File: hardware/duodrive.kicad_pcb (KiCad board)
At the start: 2 copper layers, 49 x 75 mm, 92 parts, among them J1 Power, J2 Conn_01x04, J3 Conn_01x03, J4 MP2359, J6 Conn_01x04, J7 Conn_01x04, J8 Conn_01x04, Q1 AOD4184, Q2 AOD4184, Q3 AOD4184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

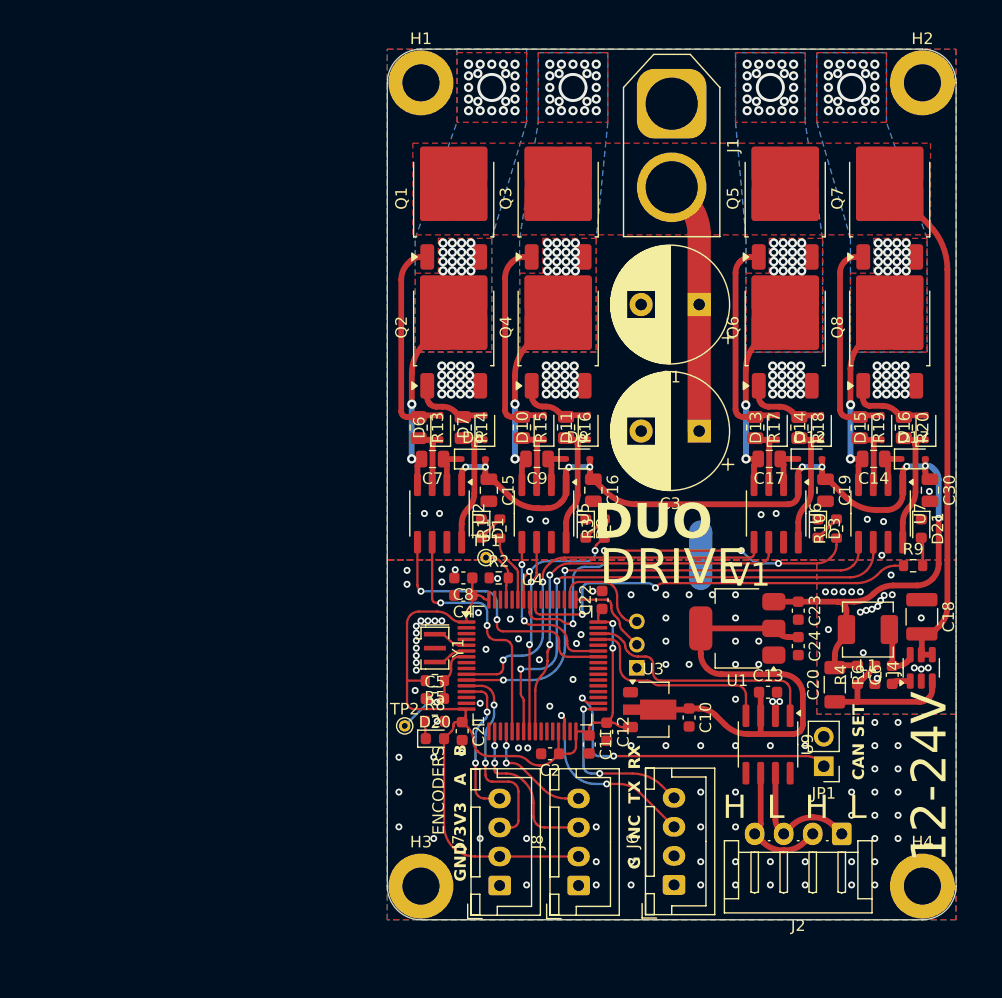
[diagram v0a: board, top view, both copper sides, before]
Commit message: Hardware bug fix
Fixed buck converter output bulk capacitor not connected to ground
Added pull up resistor at buck EN pin instead of connect it to VCC
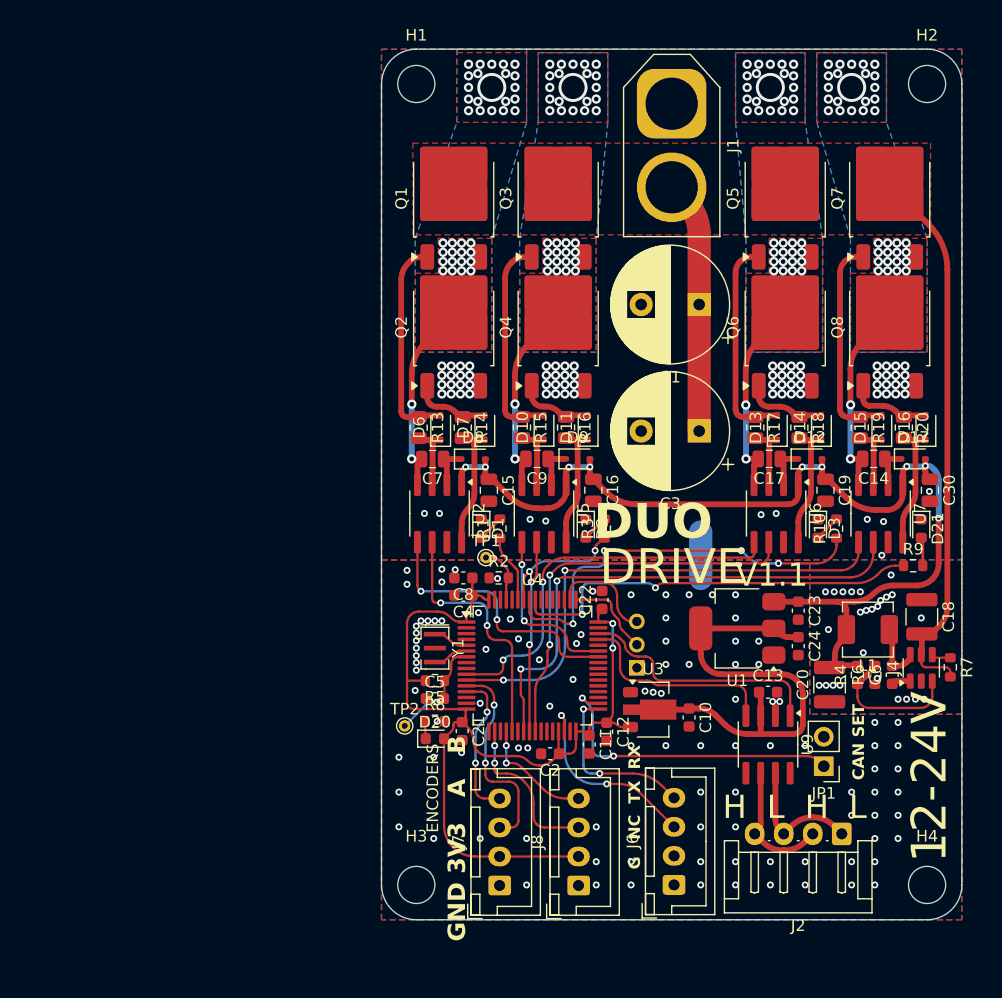
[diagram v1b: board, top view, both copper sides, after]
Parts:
- added R7: 1K, Resistor_SMD:R_0603_1608Metric, F.Cu at (168.5, 103.2)
- C20: value C -> 10uF; footprint Capacitor_SMD:C_1206_3216Metric -> Capacitor_SMD:C_1210_3225Metric
- H1, H2, H3, H4: footprint MountingHole:MountingHole_3.2mm_M3_DIN965_Pad -> MountingHole:MountingHole_3.2mm_M3
- moved C20 0.45 mm to (158.1, 104.8)
- moved H1 0.41 mm to (122.5, 53.0)
- moved H2 0.41 mm to (166.5, 53.0)
- moved H3 0.41 mm to (122.5, 122.0)
- moved H4 0.41 mm to (166.5, 122.0)
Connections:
- C20 pad 1: Net-(J4-Pin_3) -> GND
- J4 pad 4: VDC -> Net-(J4-Pin_4)
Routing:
- net VDC: track 63.8 -> 66.9 mm
- net Net-(J4-Pin_4): track 0.00 -> 1.81 mm
- net Net-(J4-Pin_3): track 13.5 -> 12.1 mm
- net GNDS: vias 99 -> 102
- net GND: vias 94 -> 99
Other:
- board size 49 x 75 mm -> 50 x 75 mm
- board text added: "V1.1"
- board text removed: "V1"

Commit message: Minor bug fix and QOL feature
Minor bug fix:
- Changed layout of buck converter for bigger capacitor and added pull up resistor
- Fixed buck output capacitor connected to wrong pin
- Changed passive component value to match final product value
QOL Feature:
- Added QR code on the bottom silkscreen for wiki page
- SWD connector changed from 2mm to 2.54mm for easier debug or update
- Grouping and separation in schematic layout for better visual clarity
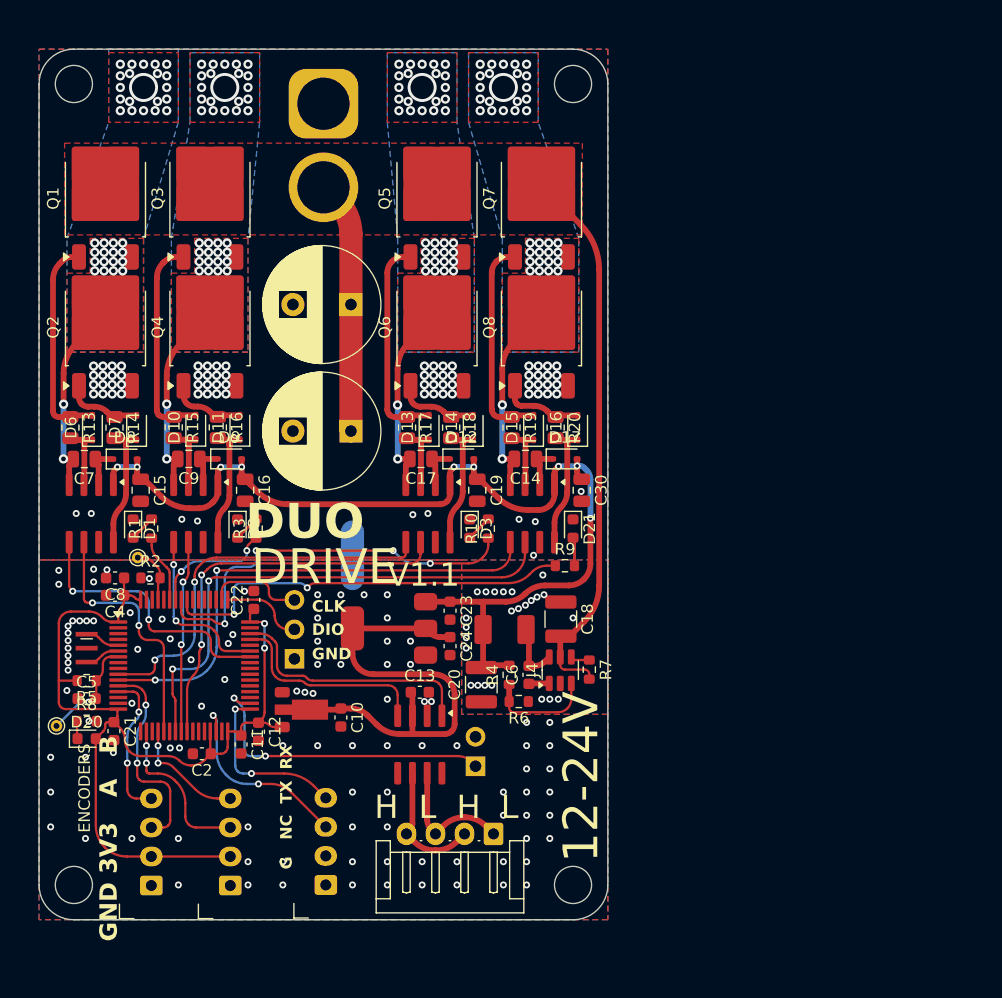
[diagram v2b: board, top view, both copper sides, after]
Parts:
- added G***: LOGO, LOGO, B.Cu at (114.5, 90.3)
- C1, C3: value 1000uF -> 680uF
- C18, C20: value 10uF -> 22uF
- J3: footprint Connector_PinHeader_2.00mm:PinHeader_1x03_P2.00mm_Vertical -> Connector_PinHeader_2.54mm:PinHeader_1x03_P2.54mm_Vertical
- R4: value 11K -> 11.8K
- R7: value 1K -> 10K
- U1: footprint Package_TO_SOT_SMD:SOT-223-3_TabPin2 -> 1_NoOutline:SOT-223-3_TabPin2
- U2, U5, U6, U7, U9: footprint Package_SO:SOIC-8_3.9x4.9mm_P1.27mm -> 1_NoOutline:SOIC-8_3.9x4.9mm_P1.27mm
- U3: value HT75xx-1-SOT89 -> HT7833; footprint Package_TO_SOT_SMD:SOT-89-3 -> 1_NoOutline:SOT-89-3
- moved C6 31.3 mm to (132.2, 103.9)
- moved L1 31.3 mm to (130.1, 100.0)
- moved C18 31.1 mm to (135.0, 99.1)
- moved J4 31.1 mm to (134.9, 103.5)
- moved R7 31.1 mm to (137.4, 103.5)
- moved R6 30.8 mm to (131.3, 106.2), turned to 180 degrees
- moved H2 30.5 mm to (136.0, 53.0)
- moved H4 30.5 mm to (136.0, 122.0)
- moved C13 30.0 mm to (122.8, 105.4)
- moved D11 30.0 mm to (107.3, 82.6)
- moved J7 30.0 mm to (99.7, 122.0)
- moved U9 30.0 mm to (122.8, 109.9)
- moved C10 30.0 mm to (116.0, 107.6)
- moved C11 30.0 mm to (107.4, 109.9)
- moved C12 30.0 mm to (108.9, 108.8)
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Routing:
- net Net-(J4-Pin_3): track 12.1 -> 9.56 mm
- net SWCLK: track 9.19 -> 8.42 mm
- net VDC: track 66.9 -> 67.6 mm
- net +10V: track 91.7 -> 91.2 mm
- net GNDS: vias 102 -> 101
- net GND: vias 99 -> 98
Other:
- board size 50 x 75 mm -> 49 x 75 mm
- board text added: "CLK"
- board text added: "DIO"
- board text added: "GND"
- board text added: "MADE BY"
- board text added: "MANH"
- board text added: "TI"
- board text added: "WIKI PAGE"
- board text removed: "CAN SET"

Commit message: NEW Version
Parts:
- removed J2: Conn_01x04, Connector_JST:JST_EH_S4B-EH_1x04_P2.50mm_Horizontal
- removed J4: MP2359, Package_TO_SOT_SMD:SOT-23-6
- removed J6: Conn_01x04, Connector_JST:JST_XH_B4B-XH-A_1x04_P2.50mm_Vertical
- removed JP1: CANBUS, Connector_PinHeader_2.54mm:PinHeader_1x02_P2.54mm_Vertical
- removed U3: HT7833, 1_NoOutline:SOT-89-3
- added C25: 33nF, Capacitor_SMD:C_0603_1608Metric, F.Cu at (133.6, 105.5)
- added C26: 470pF, Capacitor_SMD:C_0603_1608Metric, F.Cu at (110.7, 106.5)
- added C27: 22uF, Capacitor_SMD:C_1206_3216Metric, F.Cu at (134.9, 98.6)
- added C28: 22uF, Capacitor_SMD:C_1206_3216Metric, F.Cu at (129.0, 98.8)
- added J10: Power, TerminalBlock_Phoenix:TerminalBlock_Phoenix_PT-1,5-2-3.5-H_1x02_P3.50mm_Horizontal, F.Cu at (127.5, 51.4)
- added J12: Conn_02x09_Odd_Even, Connector_PinHeader_2.54mm:PinHeader_2x08_P2.54mm_Horizontal, F.Cu at (130.6, 111.9)
- added J9: Power, TerminalBlock_Phoenix:TerminalBlock_Phoenix_PT-1,5-2-3.5-H_1x02_P3.50mm_Horizontal, F.Cu at (105.0, 51.4)
- added JP2: Jumper_3_Open, Connector_PinHeader_2.54mm:PinHeader_1x03_P2.54mm_Vertical, F.Cu at (93.8, 116.3)
- added R11: 1K, Resistor_SMD:R_0603_1608Metric, F.Cu at (136.5, 105.5)
- added R12: 10K, Resistor_SMD:R_0603_1608Metric, F.Cu at (136.5, 102.5)
- added U10: MIC5219-3.3YM5, Package_TO_SOT_SMD:SOT-23-5, F.Cu at (113.6, 106.5)
- added U8: TPS62933, Package_TO_SOT_SMD:SOT-583-8, F.Cu at (132.8, 102.5)
- C18, C20: footprint Capacitor_SMD:C_1210_3225Metric -> Capacitor_SMD:C_1206_3216Metric
- C6: value 10nF -> 100nF
- D10, D11, D12, D13, D14, D15, D16, D17, D6, D7, D8, D9: footprint Diode_SMD:D_SOD-323 -> Diode_SMD:D_0805_2012Metric
- J3: moved to F.Cu
- L1: value 4.7uH -> 12uH; footprint Inductor_SMD:L_Changjiang_FXL0420 -> Inductor_SMD:L_APV_ANR4020
- moved R8 7.25 mm to (91.1, 114.5), turned to -90 degrees
- moved C13 5.43 mm to (117.5, 106.6), turned to 90 degrees
- moved L1 4.83 mm to (129.0, 104.7)
- moved R4 4.27 mm to (129.0, 107.9), turned to 180 degrees
- moved C20 3.66 mm to (129.0, 101.2), turned to 180 degrees
- moved D20 3.61 mm to (91.1, 111.4), turned to 90 degrees
- moved U9 3.40 mm to (122.0, 106.6), turned to 0 degrees
- moved C10 2.79 mm to (113.6, 109.0), turned to 180 degrees
- moved R7 2.68 mm to (134.9, 102.5)
- moved C18 2.40 mm to (132.6, 98.6)
- moved R6 1.91 mm to (132.2, 107.9)
- moved C6 1.60 mm to (132.1, 105.5)
- moved TP2 0.76 mm to (91.2, 107.6)
- moved J8 0.33 mm to (106.8, 122.0)
- turned J3 to 180 degrees
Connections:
- C6 pad 1: Net-(J4-Pin_1) -> Net-(U8-SW)
- C6 pad 2: Net-(J4-Pin_6) -> Net-(U8-BST)
- J7 pad 2: +3.3V -> VBUS
- J8 pad 2: +3.3V -> VBUS
- L1 pad 1: Net-(J4-Pin_6) -> Net-(U8-SW)
- U9 pad 6: Net-(J2-Pin_2) -> unconnected-(U9-CANL-Pad6)
- U9 pad 7: Net-(J2-Pin_1) -> unconnected-(U9-CANH-Pad7)
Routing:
- net VDC: track 67.6 -> 46.2 mm
- net CANSET: track 26.8 -> 8.56 mm
- net CANRX: track 17.8 -> 0.00 mm
- net VBUS: track 0.00 -> 16.9 mm
- net +3.3V: track 82.8 -> 70.2 mm
- net Net-(J2-Pin_2): track 11.2 -> 0.00 mm
- net Net-(J2-Pin_1): track 11.2 -> 0.00 mm
- net +5V: track 43.7 -> 33.6 mm
- net CANTX: track 22.0 -> 12.1 mm
- net RX: track 15.0 -> 7.99 mm
- net TX: track 17.1 -> 10.2 mm
- net Net-(J4-Pin_6): track 5.39 -> 0.00 mm
- net Net-(U8-RT): track 0.00 -> 4.86 mm
- net Net-(U8-EN): track 1.75 -> 4.16 mm
- net Net-(U10-BP): track 0.00 -> 1.83 mm
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- added copper zone on F.Cu, net Net-(U8-SW)
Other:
- board text added: "V2.1"
- board text removed: "12-24V"
- board text removed: "ENCODERS"
- board text removed: "G NC TX RX"
- board text removed: "H L H L"
- board text removed: "V1.1"

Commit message: pcb
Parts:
- removed C23, C24: 10uF, Capacitor_SMD:C_0603_1608Metric
- removed J12: Conn_02x09_Odd_Even, Connector_PinHeader_2.54mm:PinHeader_2x08_P2.54mm_Horizontal
- removed U1: AMS1117-5.0, 1_NoOutline:SOT-223-3_TabPin2
- added C29: 10uF, Capacitor_SMD:C_0805_2012Metric, F.Cu at (125.6, 100.3)
- added C31: 22uF, Capacitor_SMD:C_0805_2012Metric, F.Cu at (122.8, 101.1)
- added C41: 100nF, Capacitor_SMD:C_0603_1608Metric, F.Cu at (124.8, 96.8)
- added C42: 100nF, Capacitor_SMD:C_0603_1608Metric, F.Cu at (119.0, 97.5)
- added J2: Conn_02x08_Odd_Even, Connector_PinHeader_2.54mm:PinHeader_2x08_P2.54mm_Horizontal, F.Cu at (130.6, 111.8)
- added L2: 2.2uH, Inductor_SMD_Wurth:L_Wurth_WE-LQSH-3012, F.Cu at (119.3, 100.2)
- added REF**: C_0402_1005Metric, Capacitor_SMD:C_0402_1005Metric, F.Cu at (147.2, 104.0)
- added U3: TPS62173DSG, Package_SON:WSON-8-1EP_2x2mm_P0.5mm_EP0.9x1.6mm_ThermalVias, F.Cu at (122.8, 98.8)
- moved NT1 3.00 mm to (114.0, 93.6)
- moved C21 1.11 mm to (95.6, 108.0), turned to 180 degrees
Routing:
- net +5V: track 33.6 -> 40.5 mm, vias 0 -> 2
- net +10V: track 90.7 -> 97.4 mm
- net CANRX: track 0.00 -> 5.02 mm
- net PWM2A: track 13.0 -> 15.3 mm
- net CANTX: track 12.1 -> 14.0 mm
- net PWM1A: track 16.4 -> 18.2 mm
- net VBUS: track 16.9 -> 18.2 mm
- net PWM1B: track 12.0 -> 13.0 mm
- net PWM2B: track 10.7 -> 11.5 mm
- net GNDS: vias 32 -> 33
- net GND: vias 74 -> 100
- added copper zone on F.Cu, net +5V
- added copper zone on F.Cu, net Net-(U3-SW)
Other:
- board text added: "CHA"
- board text added: "CHB"
- board text added: "VDC"
- board text removed: "GND 3V3 A B"

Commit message: test
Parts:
- removed REF**: C_0402_1005Metric, Capacitor_SMD:C_0402_1005Metric
- added J4: Conn_01x04, Connector_JST:JST_SH_SM04B-SRSS-TB_1x04-1MP_P1.00mm_Horizontal, F.Cu at (135.7, 106.7)
- added J5: Conn_01x04, Connector_JST:JST_SH_SM04B-SRSS-TB_1x04-1MP_P1.00mm_Horizontal, F.Cu at (135.7, 114.5)
- moved C28 8.34 mm to (128.2, 107.1)
- moved C27 6.75 mm to (128.2, 97.8), turned to 0 degrees
- moved R11 5.25 mm to (134.9, 100.5), turned to 180 degrees
- moved C25 3.73 mm to (134.9, 102.0), turned to 180 degrees
- moved R7 3.57 mm to (134.9, 98.9), turned to 180 degrees
- moved J3 2.40 mm to (114.4, 102.5)
- moved R4 2.00 mm to (127.4, 109.1)
- moved R6 2.00 mm to (130.6, 109.1)
- moved R12 1.45 mm to (137.2, 101.2)
- moved C18 1.27 mm to (131.8, 97.6)
- moved C20 1.27 mm to (128.2, 100.2)
- moved C6 1.27 mm to (131.3, 104.5)
- moved L1 1.27 mm to (128.2, 103.7)
- moved U8 1.27 mm to (132.0, 101.5)
- moved C31 1.22 mm to (121.6, 101.3)
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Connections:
- J2 pad 1: unconnected-(J2-Pin_1-Pad1) -> GNDS
- J2 pad 10: unconnected-(J2-Pin_10-Pad10) -> PC6
- J2 pad 11: unconnected-(J2-Pin_11-Pad11) -> SPI_MOSI
- J2 pad 12: unconnected-(J2-Pin_12-Pad12) -> SPI_MISO
- J2 pad 13: unconnected-(J2-Pin_13-Pad13) -> SPI_CLK
- J2 pad 14: unconnected-(J2-Pin_14-Pad14) -> +3.3V
- J2 pad 15: unconnected-(J2-Pin_15-Pad15) -> RX
- J2 pad 16: unconnected-(J2-Pin_16-Pad16) -> TX
- J2 pad 3: unconnected-(J2-Pin_3-Pad3) -> PA9
- J2 pad 4: unconnected-(J2-Pin_4-Pad4) -> PA8
- J2 pad 5: unconnected-(J2-Pin_5-Pad5) -> PC9
- J2 pad 6: unconnected-(J2-Pin_6-Pad6) -> PC8
- J2 pad 7: unconnected-(J2-Pin_7-Pad7) -> GNDS
- J2 pad 8: unconnected-(J2-Pin_8-Pad8) -> +5V
- J2 pad 9: unconnected-(J2-Pin_9-Pad9) -> PC7
- U4 pad 35: unconnected-(U4-PB13-Pad35) -> SPI_CLK
- U4 pad 36: unconnected-(U4-PB14-Pad36) -> SPI_MISO
- U4 pad 37: unconnected-(U4-PB15-Pad37) -> SPI_MOSI
- U4 pad 38: unconnected-(U4-PC6-Pad38) -> PC6
- U4 pad 39: unconnected-(U4-PC7-Pad39) -> PC7
- U4 pad 40: unconnected-(U4-PC8-Pad40) -> PC8
- U4 pad 41: unconnected-(U4-PC9-Pad41) -> PC9
- U4 pad 42: H1 -> PA8
- U4 pad 43: H2 -> PA9
- U4 pad 8: unconnected-(U4-PC0-Pad8) -> H1
- U4 pad 9: unconnected-(U4-PC1-Pad9) -> H2
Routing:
- net +5V: track 40.5 -> 78.1 mm
- net PA8: track 0.00 -> 26.0 mm, vias 0 -> 1
- net PA9: track 0.00 -> 24.0 mm, vias 0 -> 1
- net +10V: track 97.4 -> 74.2 mm
- net PC8: track 0.00 -> 23.1 mm, vias 0 -> 1
- net PC9: track 0.00 -> 21.2 mm, vias 0 -> 1
- net PC6: track 0.00 -> 18.2 mm, vias 0 -> 1
- net PC7: track 0.00 -> 16.2 mm, vias 0 -> 1
- net SPI_MISO: track 0.00 -> 14.5 mm, vias 0 -> 1
- net CANRX: track 5.02 -> 18.0 mm
- net SPI_MOSI: track 0.00 -> 12.6 mm, vias 0 -> 1
- net SPI_CLK: track 0.00 -> 10.4 mm, vias 0 -> 1
- net VDC: track 46.2 -> 36.2 mm
- net Net-(U8-FB): track 9.16 -> 0.00 mm
- net H1: track 24.2 -> 15.2 mm
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
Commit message: layout
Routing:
- net PC7: track 16.2 -> 15.6 mm
- net PC6: track 18.2 -> 17.6 mm
- net Reset: track 10.7 -> 10.1 mm

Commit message: layout update
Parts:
- removed J1: Power, Connector_AMASS:AMASS_XT60-M_1x02_P7.20mm_Vertical
- removed J10, J9: Power, TerminalBlock_Phoenix:TerminalBlock_Phoenix_PT-1,5-2-3.5-H_1x02_P3.50mm_Horizontal
- added C15: 100nF, Capacitor_SMD:C_0603_1608Metric, F.Cu at (99.3, 66.0)
- added C15: 100nF, Capacitor_SMD:C_0603_1608Metric, F.Cu at (130.2, 66.0)
- added C15: 100nF, Capacitor_SMD:C_0603_1608Metric, F.Cu at (121.6, 66.3)
- added C15: 100nF, Capacitor_SMD:C_0603_1608Metric, F.Cu at (107.9, 66.0)
- added C27: 22uF, Capacitor_SMD:C_1206_3216Metric, F.Cu at (97.8, 55.8)
- added C27: 22uF, Capacitor_SMD:C_1206_3216Metric, F.Cu at (131.2, 55.8)
- added J6: Conn_01x06, TerminalBlock_MetzConnect:TerminalBlock_MetzConnect_Type094_RT03506HBLU_1x06_P5.00mm_Horizontal, F.Cu at (102.0, 53.5)
- C1, C3: footprint Capacitor_THT:CP_Radial_D10.0mm_P5.00mm -> Capacitor_SMD:C_Elec_10x10.2
- C15, C16, C19, C30: footprint Capacitor_SMD:C_0805_2012Metric -> Capacitor_SMD:C_0603_1608Metric
- moved C1 6.45 mm to (114.5, 66.0), turned to -90 degrees
- moved C3 5.08 mm to (114.5, 78.4), turned to 0 degrees
- moved C16 1.96 mm to (105.8, 88.2)
- moved Q5 1.62 mm to (125.9, 62.9)
- moved Q6 1.62 mm to (125.9, 74.0)
- moved C15 1.56 mm to (97.2, 88.2)
- moved C9 1.40 mm to (101.5, 85.3)
- moved D9 1.30 mm to (105.1, 85.3)
- moved D2 1.30 mm to (105.8, 91.3)
- moved R3 1.30 mm to (107.4, 91.3)
- moved Q8 1.22 mm to (134.5, 74.0)
- moved Q7 1.22 mm to (134.5, 62.9)
- moved D10 1.20 mm to (102.3, 82.6)
- moved D11 1.20 mm to (106.1, 82.6)
- moved R16 1.20 mm to (104.2, 82.6)
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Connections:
- net Net-(J10-Pin_1) renamed MOTOR_OUT_4
- net Net-(J10-Pin_2) renamed MOTOR_OUT_3
- net Net-(J9-Pin_1) renamed MOTOR_OUT_2
- net Net-(J9-Pin_2) renamed MOTOR_OUT_1
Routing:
- net +10V: track 74.2 -> 4.68 mm, vias 9 -> 0
- net Net-(D13-A): track 18.7 -> 0.00 mm
- net Net-(D15-A): track 18.7 -> 0.00 mm
- net Net-(D10-A): track 18.7 -> 0.00 mm
- net Net-(D6-A): track 18.6 -> 0.00 mm
- net MOTOR_OUT_2: track 15.2 -> 0.00 mm, vias 43 -> 131
- net MOTOR_OUT_3: track 15.1 -> 0.00 mm, vias 43 -> 131
- net MOTOR_OUT_4: track 15.1 -> 0.00 mm, vias 44 -> 131
- net MOTOR_OUT_1: track 15.0 -> 0.00 mm, vias 43 -> 131
- net Net-(D16-K): track 11.2 -> 0.00 mm
- net Net-(D7-K): track 11.2 -> 0.00 mm
- net Net-(D14-K): track 11.2 -> 0.00 mm
- net Net-(D11-K): track 11.2 -> 0.00 mm
- net +5V: track 78.1 -> 68.2 mm
- net Net-(D16-A): track 7.39 -> 0.00 mm
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- added copper zone on B.Cu, net VDC

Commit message: update
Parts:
- removed the C15 at (99.3, 66.0)
- removed the C15 at (130.2, 66.0)
- removed the C15 at (121.6, 66.3)
- removed the C15 at (107.9, 66.0)
- removed the C27 at (97.8, 55.8)
- removed the C27 at (131.2, 55.8)
- added C23: 22uF, Capacitor_SMD:C_1206_3216Metric, F.Cu at (131.2, 55.8)
- added C24: 22uF, Capacitor_SMD:C_1206_3216Metric, F.Cu at (97.8, 55.8)
- added C32: 1uF, Capacitor_SMD:C_0603_1608Metric, F.Cu at (99.3, 66.0)
- added C33: 1uF, Capacitor_SMD:C_0603_1608Metric, F.Cu at (107.9, 66.0)
- added C34: 1uF, Capacitor_SMD:C_0603_1608Metric, F.Cu at (130.2, 66.0)
- added C35: 1uF, Capacitor_SMD:C_0603_1608Metric, F.Cu at (121.6, 66.0)
- moved TP1 0.60 mm to (97.5, 93.8)
- moved C19 0.30 mm to (128.5, 88.2)
- moved C30 0.30 mm to (137.0, 88.3)
- moved C15 0.30 mm to (97.5, 88.2)
- moved C16 0.30 mm to (106.1, 88.2)
- moved C17 0.10 mm to (123.9, 85.3)
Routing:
- net +10V: track 4.68 -> 64.2 mm, vias 0 -> 8
- net Net-(D6-A): track 0.00 -> 17.7 mm
- net Net-(D15-A): track 0.00 -> 17.5 mm
- net Net-(D13-A): track 0.00 -> 17.4 mm
- net Net-(D10-A): track 0.00 -> 17.1 mm
- net MOTOR_OUT_4: track 0.00 -> 16.6 mm, vias 131 -> 178
- net MOTOR_OUT_2: track 0.00 -> 16.6 mm, vias 131 -> 178
- net MOTOR_OUT_1: track 0.00 -> 16.6 mm, vias 131 -> 178
- net MOTOR_OUT_3: track 0.00 -> 16.5 mm, vias 131 -> 178
- net Net-(D16-K): track 0.00 -> 11.6 mm
- net Net-(D7-K): track 0.00 -> 11.6 mm
- net Net-(D14-K): track 0.00 -> 11.6 mm
- net Net-(D11-K): track 0.00 -> 11.6 mm
- net Net-(D11-A): track 0.00 -> 6.64 mm
- net Net-(D7-A): track 0.00 -> 6.64 mm
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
